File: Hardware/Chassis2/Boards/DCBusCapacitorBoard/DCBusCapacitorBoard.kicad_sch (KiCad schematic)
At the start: 16 parts

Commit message: Update Powerstage dc cap board
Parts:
- added H3, H6: MountingHole_Pad, MountingHole:MountingHole_6.4mm_M6_ISO14580_Pad, symbol Mechanical:MountingHole_Pad
- H4, H5: footprint MountingHole:MountingHole_3.2mm_M3_ISO14580_Pad -> MountingHole:MountingHole_6.4mm_M6_ISO14580_Pad
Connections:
- net CHASSIS_GND is gone; now on net DC_LINK_-: H4.1
- net CHASSIS_GND_1 is gone; now on net DC_LINK_+: H5.1
- net DC_LINK_+: now also H3.1
- net DC_LINK_-: now also H6.1
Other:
- moved on the sheet: H2

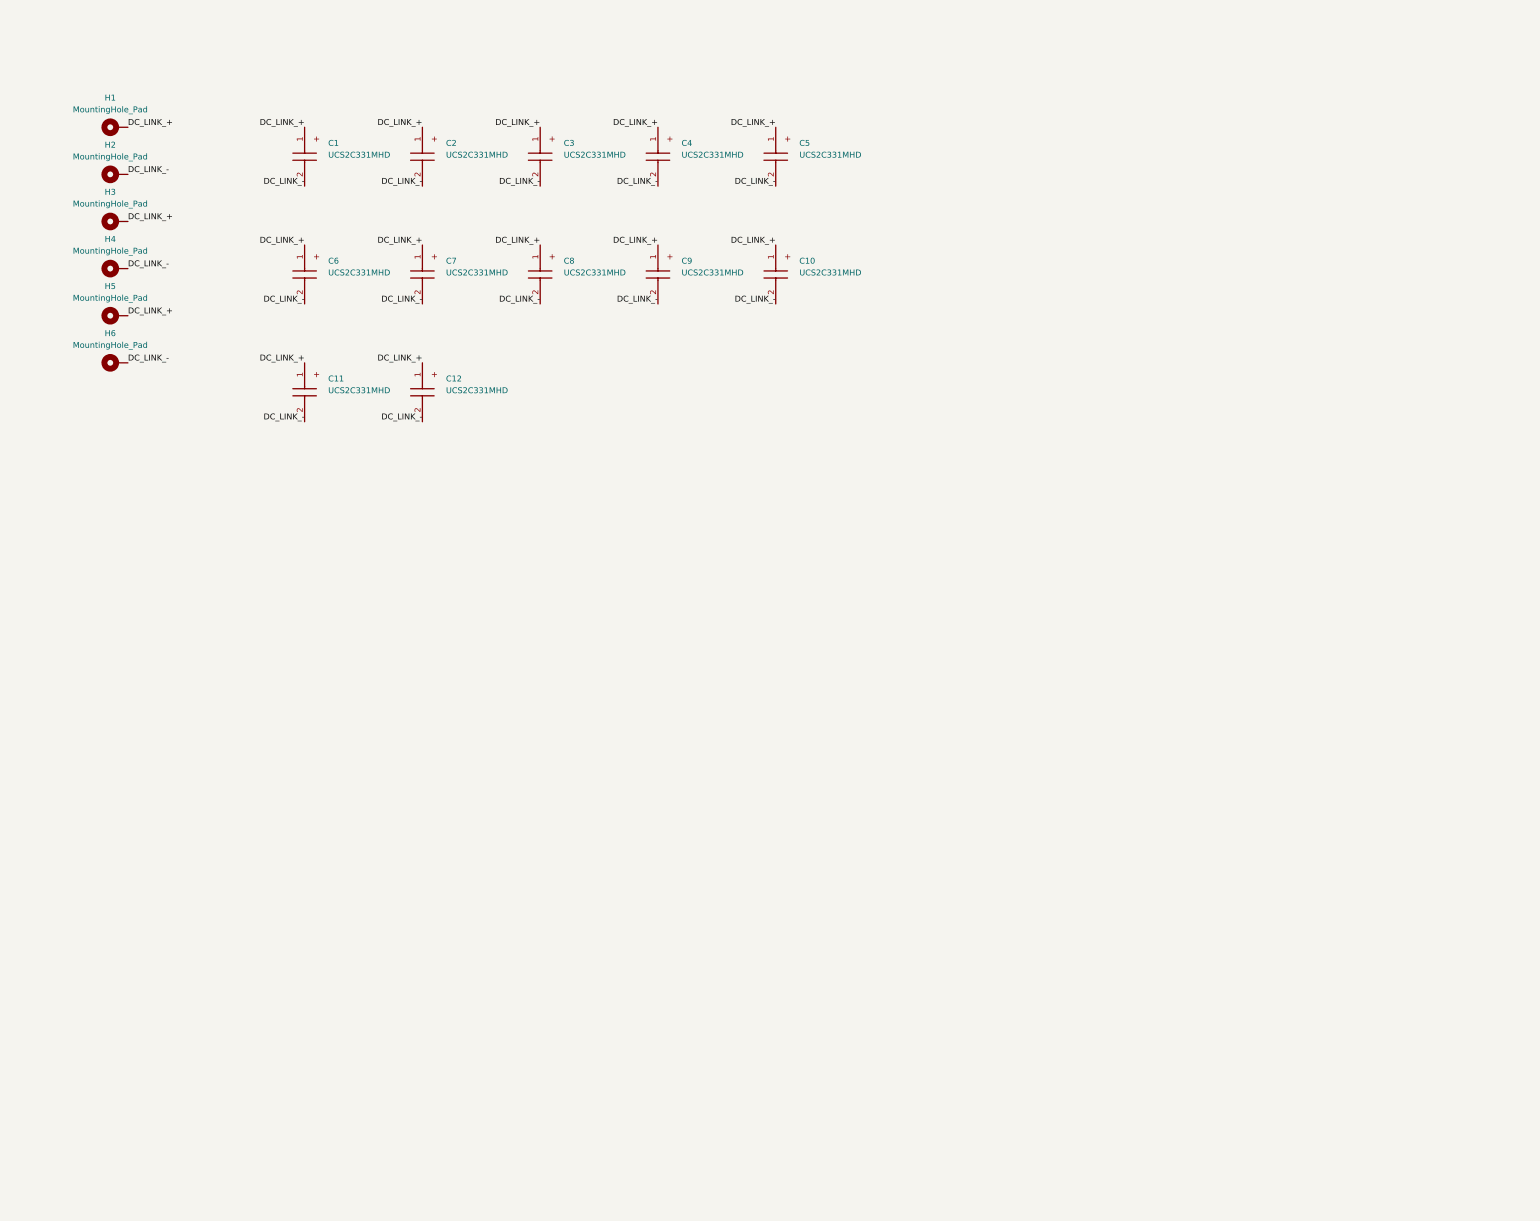
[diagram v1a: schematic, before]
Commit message: Powerstage intermediate rework
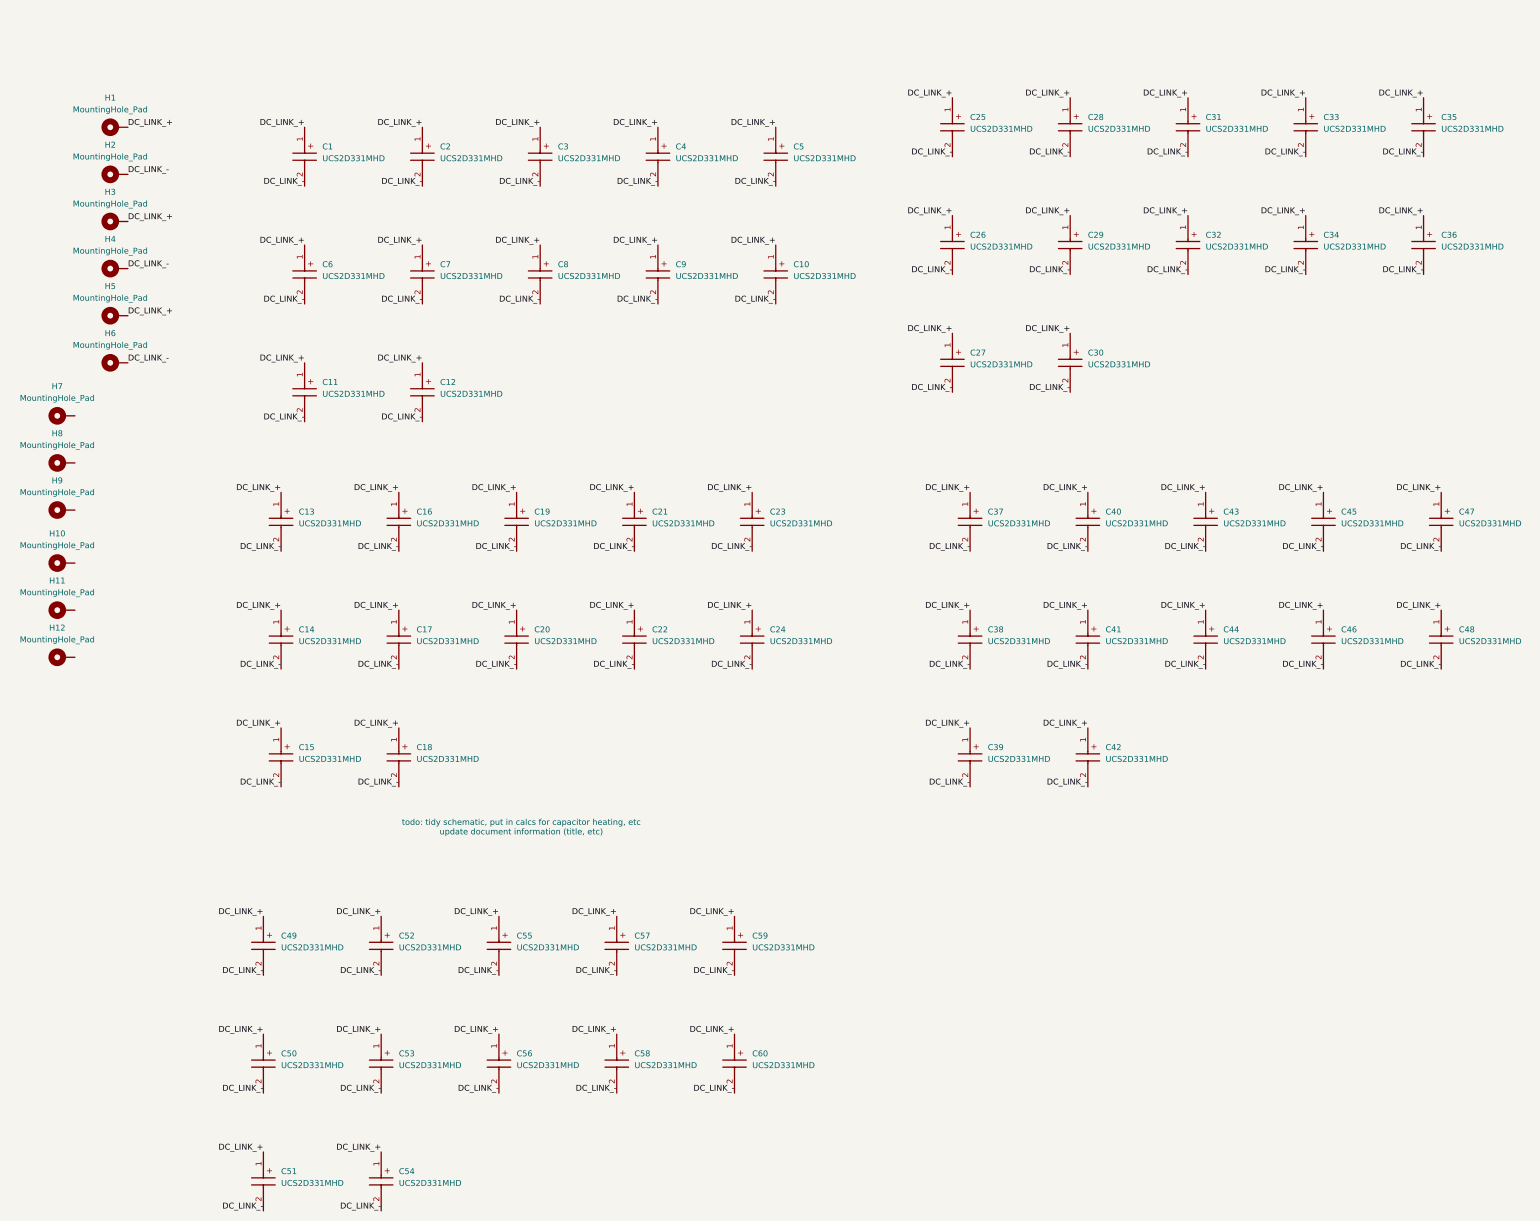
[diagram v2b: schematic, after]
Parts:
- removed C1, C10, C11, C12, C2, C3, C4, C5, C6, C7, C8, C9: UCS2C331MHD, CAPPRD750W80D1825H3200, symbol InverterCom:UCS2C331MHD
- added C1, C10, C11, C12, C13, C14, C15, C16, C17, C18, C19, C2, C20, C21, C22, C23, C24, C25, C26, C27, C28, C29, C3, C30, C31, C32, C33, C34, C35, C36, C37, C38, C39, C4, C40, C41, C42, C43, C44, C45, C46, C47, C48, C49, C5, C50, C51, C52, C53, C54, C55, C56, C57, C58, C59, C6, C60, C7, C8, C9: UCS2D331MHD, CAPPRD750W80D1800H3700, symbol InverterCom:UCS2D331MHD
- added H10, H11, H12, H7, H8, H9: MountingHole_Pad, MountingHole:MountingHole_6.4mm_M6_ISO14580_Pad, symbol Mechanical:MountingHole_Pad
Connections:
- net DC_LINK_+: now also C1.1 (+), C10.1 (+), C11.1 (+), C12.1 (+), C13.1 (+), C14.1 (+), C15.1 (+), C16.1 (+), C17.1 (+), C18.1 (+), C19.1 (+), C2.1 (+), C20.1 (+), C21.1 (+), C22.1 (+), C23.1 (+), C24.1 (+), C25.1 (+), C26.1 (+), C27.1 (+), C28.1 (+), C29.1 (+), C3.1 (+), C30.1 (+), C31.1 (+), C32.1 (+), C33.1 (+), C34.1 (+), C35.1 (+), C36.1 (+), C37.1 (+), C38.1 (+), C39.1 (+), C4.1 (+), C40.1 (+), C41.1 (+), C42.1 (+), C43.1 (+), C44.1 (+), C45.1 (+), C46.1 (+), C47.1 (+), C48.1 (+), C49.1 (+), C5.1 (+), C50.1 (+), C51.1 (+), C52.1 (+), C53.1 (+), C54.1 (+), C55.1 (+), C56.1 (+), C57.1 (+), C58.1 (+), C59.1 (+), C6.1 (+), C60.1 (+), C7.1 (+), C8.1 (+), C9.1 (+)
- net DC_LINK_-: now also C1.2 (-), C10.2 (-), C11.2 (-), C12.2 (-), C13.2 (-), C14.2 (-), C15.2 (-), C16.2 (-), C17.2 (-), C18.2 (-), C19.2 (-), C2.2 (-), C20.2 (-), C21.2 (-), C22.2 (-), C23.2 (-), C24.2 (-), C25.2 (-), C26.2 (-), C27.2 (-), C28.2 (-), C29.2 (-), C3.2 (-), C30.2 (-), C31.2 (-), C32.2 (-), C33.2 (-), C34.2 (-), C35.2 (-), C36.2 (-), C37.2 (-), C38.2 (-), C39.2 (-), C4.2 (-), C40.2 (-), C41.2 (-), C42.2 (-), C43.2 (-), C44.2 (-), C45.2 (-), C46.2 (-), C47.2 (-), C48.2 (-), C49.2 (-), C5.2 (-), C50.2 (-), C51.2 (-), C52.2 (-), C53.2 (-), C54.2 (-), C55.2 (-), C56.2 (-), C57.2 (-), C58.2 (-), C59.2 (-), C6.2 (-), C60.2 (-), C7.2 (-), C8.2 (-), C9.2 (-)
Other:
- note added: "todo: tidy schematic, put in calcs for capacitor heating, etc update document information (title, etc)"

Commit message: Update IO Board silkscreen, ExM pinout
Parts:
- added H13, H14, H15, H16: 9774030592R, 9774030592R, symbol InverterCom:9774030592R
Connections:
- no-connect marks 0 -> 10
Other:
- note added: "for top cover mounting"

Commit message: Update documentation
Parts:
- added H17, H18, H19, H20: 9774030592R, 9774030592R, symbol InverterCom:9774030592R
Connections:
- no-connect marks 10 -> 14
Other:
- note added: "for base plate to board compression, allows assembly to be one module"

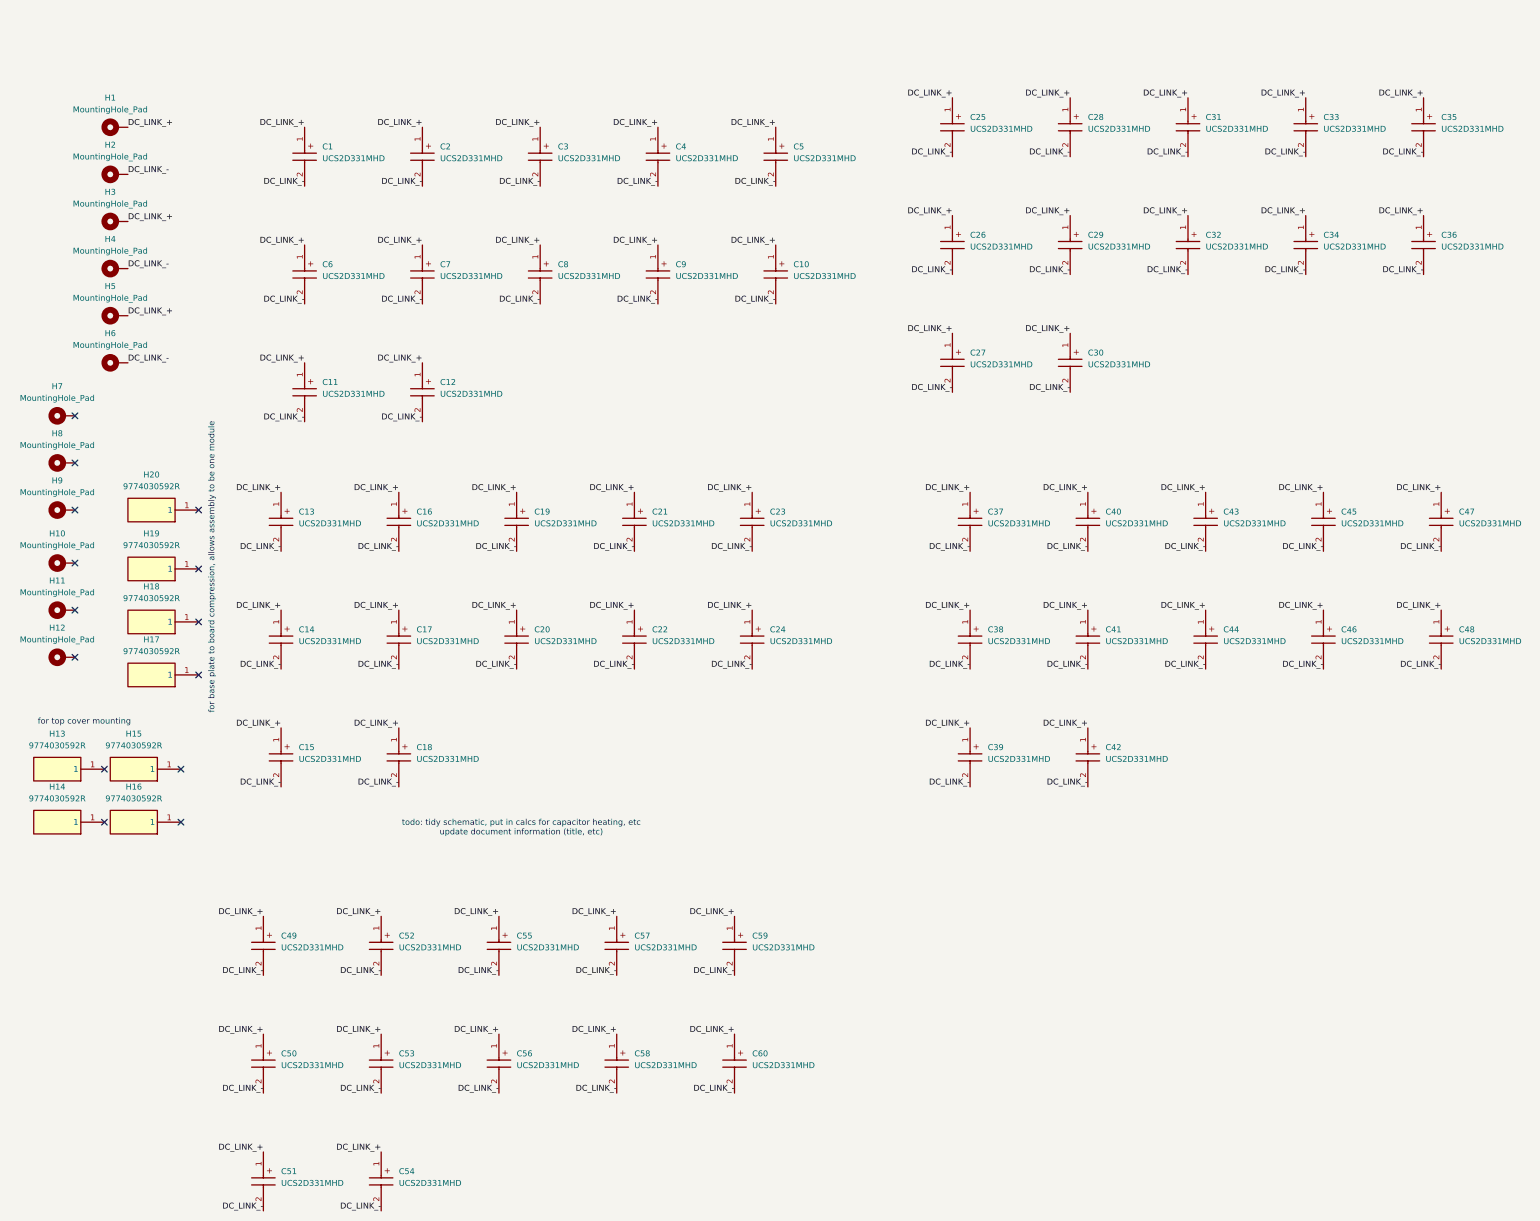
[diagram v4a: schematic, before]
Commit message: Update DC bus capacitor board
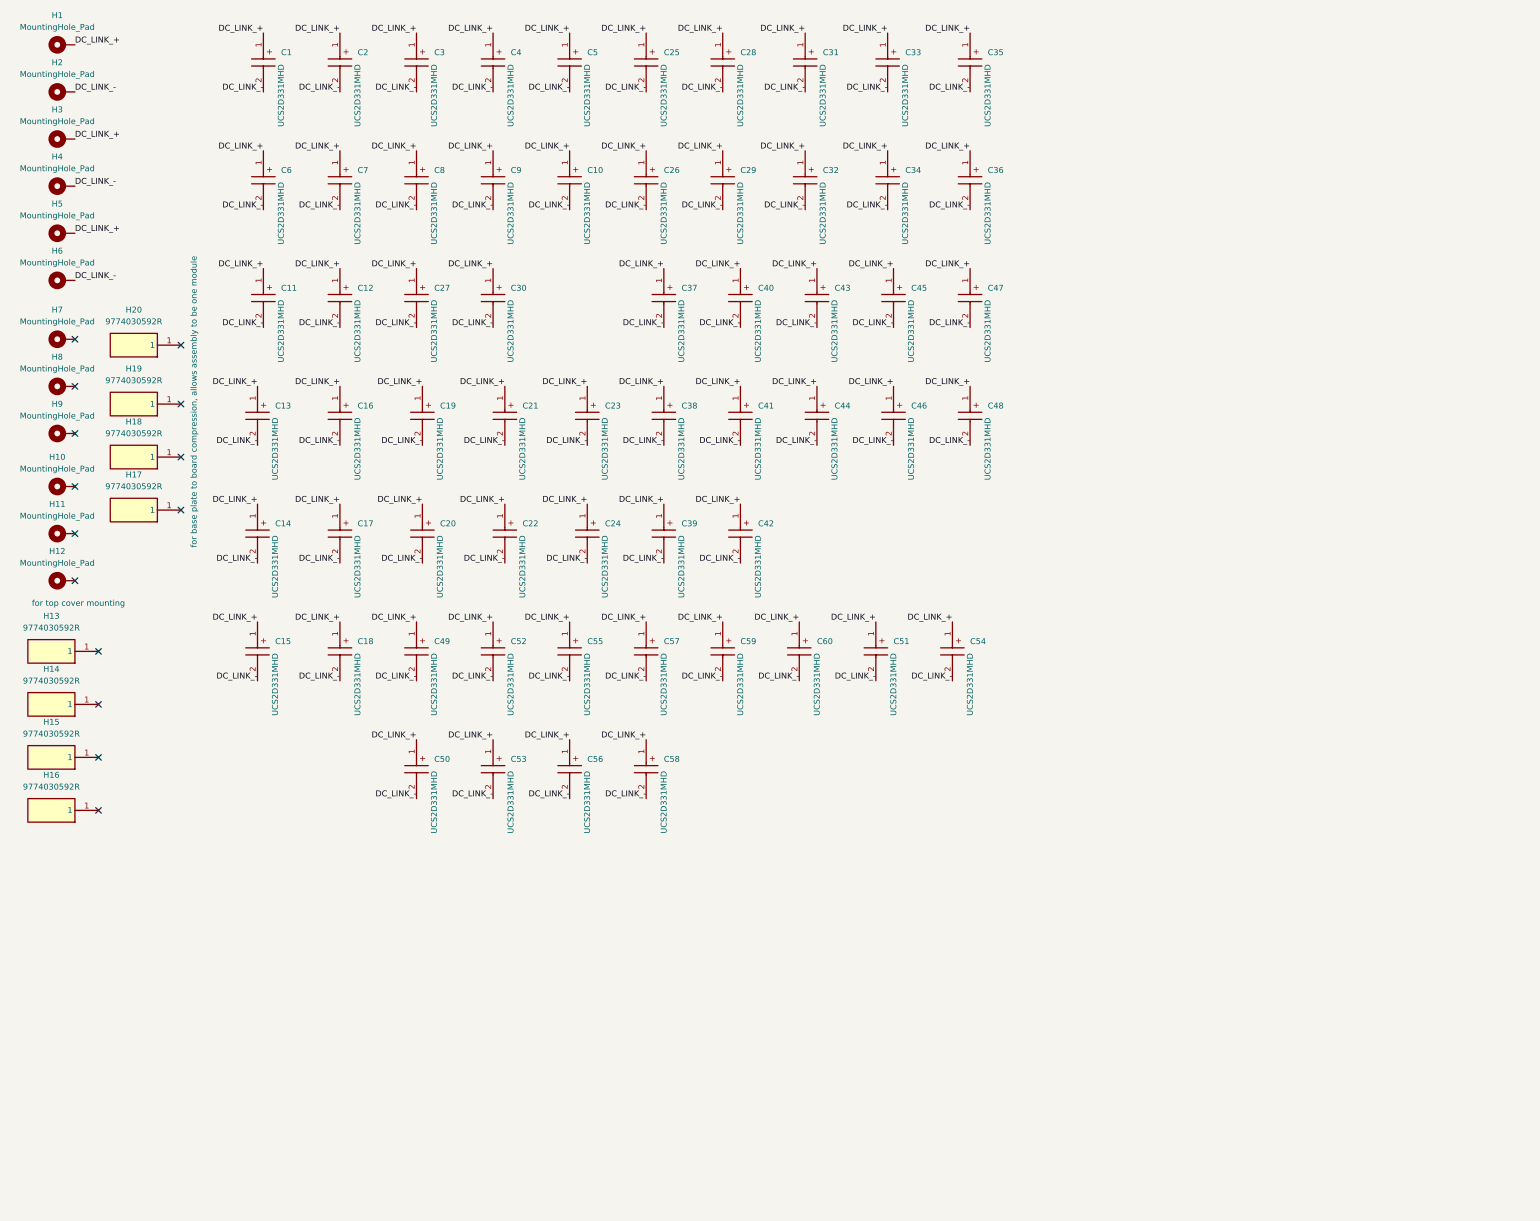
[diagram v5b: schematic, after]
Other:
- note removed: "todo: tidy schematic, put in calcs for capacitor heating, etc update document information (title, etc)"
- company: (none) -> Corzine Lab, University of California, Santa Cruz
- title: (none) -> Open Inverter Platform - DC Bus Capacitor Board
- moved on the sheet: C1, C10, C11, C12, C13, C14, C15, C16, C17, C18, C19, C2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

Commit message: Labels tool, composite board views, InverterGen5 C2 branding, even render resolution
- Labels.pdf: HV warning labels, chassis ID, per-assembly labels (label cmd)
- Board sections add composite front/back views (PCB-viewer look, mirrored
  back) and layer plots now carry the drawing sheet with true plot scale
- Branding standardized to InverterGen5 C2 (cover, footer, labels)
- STEP previews render at even resolution regardless of part aspect
- Fab part titles from info.txt PartName; ALL-CAPS handling fixed
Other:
- title: Open Inverter Platform - DC Bus Capacitor Board -> InverterGen5 - DC Bus Capacitor Board
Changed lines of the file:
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@@
 	(paper "USLetter")
 	(title_block
-		(title "Open Inverter Platform - DC Bus Capacitor Board")
+		(title "InverterGen5 - DC Bus Capacitor Board")
 		(date "2026-07-16")
 		(rev "A")
